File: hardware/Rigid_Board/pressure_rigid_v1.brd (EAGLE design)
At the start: 102.6 x 63.2 mm, 46 parts, among them M1 ARDUINO_R3_ICSP_NODIM

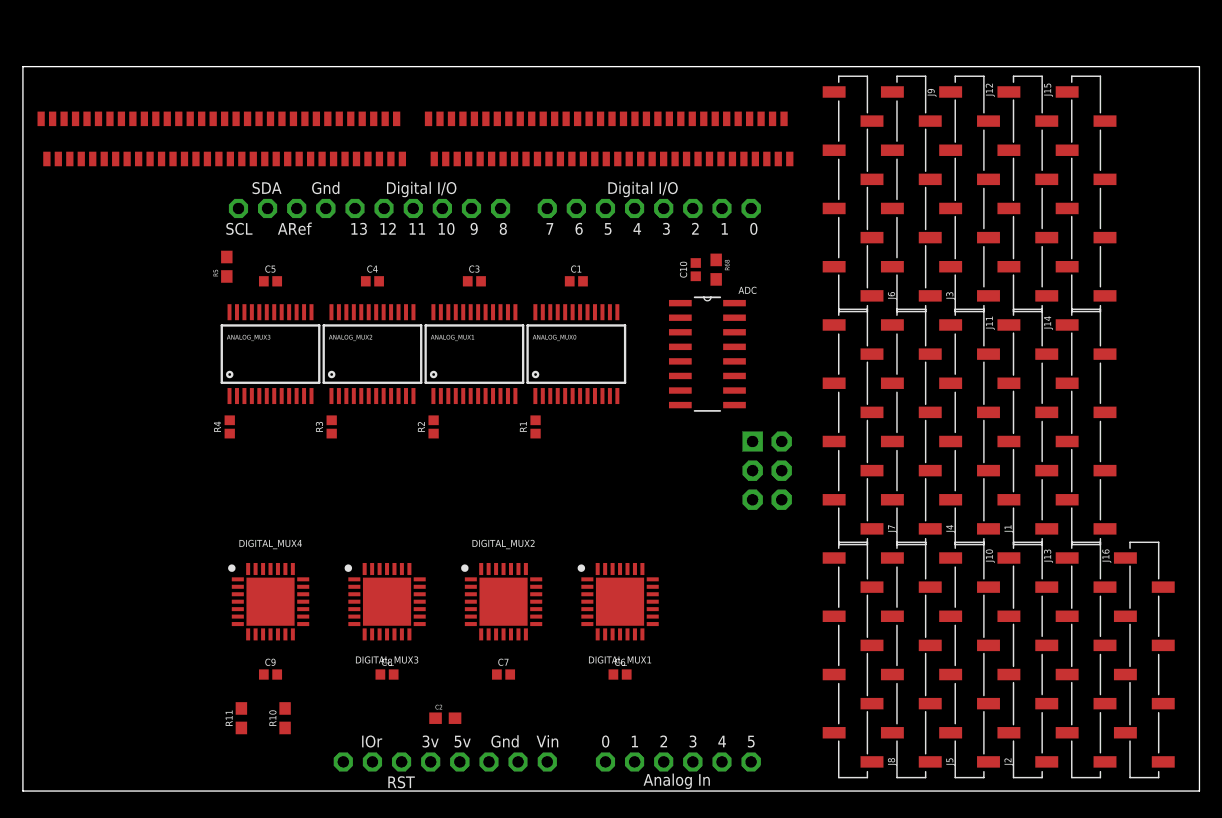
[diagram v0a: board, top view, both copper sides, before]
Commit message: Spaced out components
what
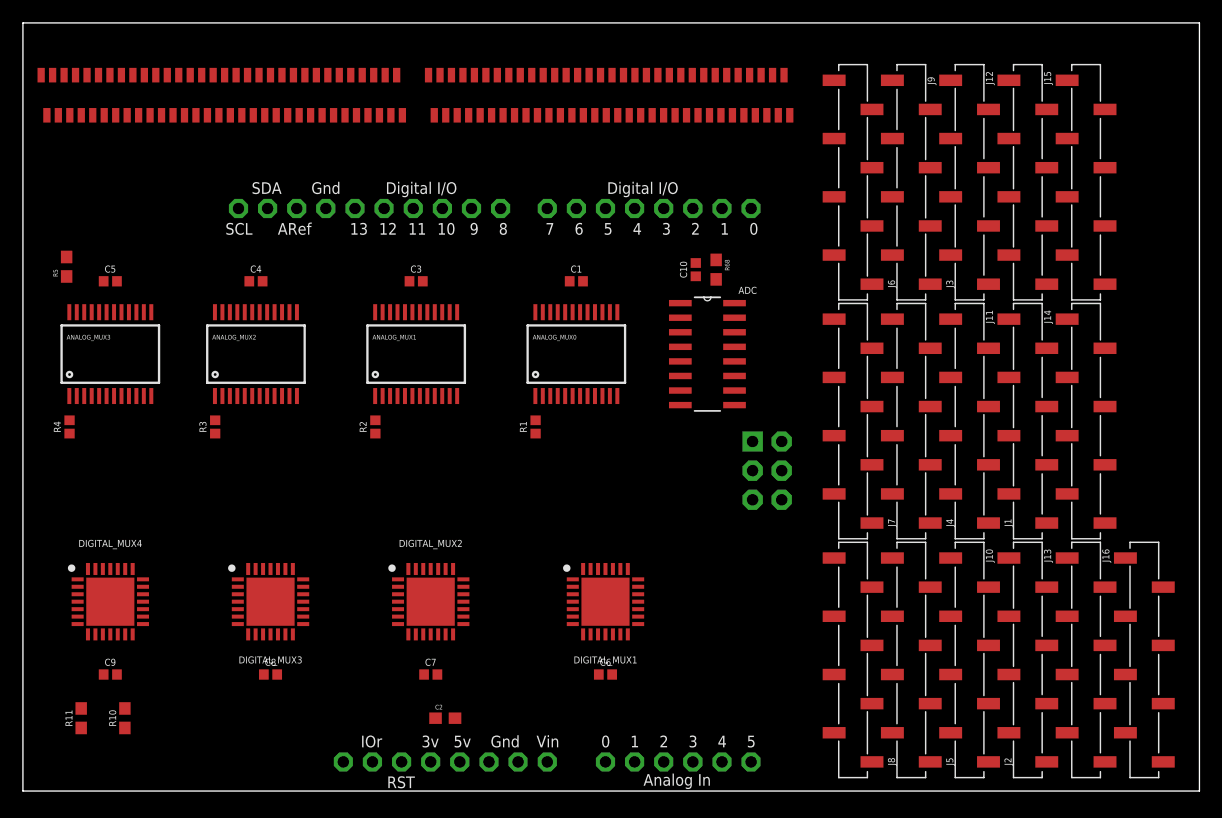
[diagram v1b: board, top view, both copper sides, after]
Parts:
- moved R11 14.0 mm to (5.08, 6.35)
- moved R5 14.0 mm to (3.81, 45.7)
- moved ANALOG_MUX3 14.0 mm to (7.62, 38.1)
- moved C5 14.0 mm to (7.62, 44.5)
- moved C9 14.0 mm to (7.62, 10.2)
- moved DIGITAL_MUX4 14.0 mm to (7.62, 16.5)
- moved R10 14.0 mm to (8.89, 6.35)
- moved R4 14.0 mm to (4.06, 31.8)
- moved ANALOG_MUX2 10.2 mm to (20.3, 38.1)
- moved C4 10.2 mm to (20.3, 44.5)
- moved C8 10.2 mm to (21.6, 10.2)
- moved DIGITAL_MUX3 10.2 mm to (21.6, 16.5)
- moved R3 10.2 mm to (16.8, 31.8)
- moved C7 6.35 mm to (35.6, 10.2)
- moved DIGITAL_MUX2 6.35 mm to (35.6, 16.5)
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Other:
- board size 102.6 x 63.2 mm -> 102.6 x 67 mm

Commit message: I'M TYPING WITH MY HANDS
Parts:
- moved J3 130.4 mm to (-27.9, 120.9)
- moved J4 130.4 mm to (-27.9, 100.1)
- moved J1 121.4 mm to (27.9, 131.8)
- moved J2 121.4 mm to (27.9, 111.0)
- moved J5 107.7 mm to (111.8, 104.6)
- moved J6 90.8 mm to (111.8, 126.0)
- moved J8 71.5 mm to (1.78, -8.89), turned to 180 degrees
- moved J7 59.3 mm to (22.6, -8.89), turned to 180 degrees
- moved J13 48.5 mm to (141.0, 24.6)
- moved J14 48.5 mm to (141.0, 45.5)
- moved J15 48.5 mm to (141.0, 66.3)
- moved J16 48.5 mm to (146.1, 24.6)
- moved J9 48.5 mm to (130.8, 66.3)
- moved J10 48.5 mm to (135.9, 24.6)
- moved J11 48.5 mm to (135.9, 45.5)
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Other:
- board size 102.6 x 67 mm -> 114.5 x 113.5 mm
